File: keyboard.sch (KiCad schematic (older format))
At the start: 14 parts

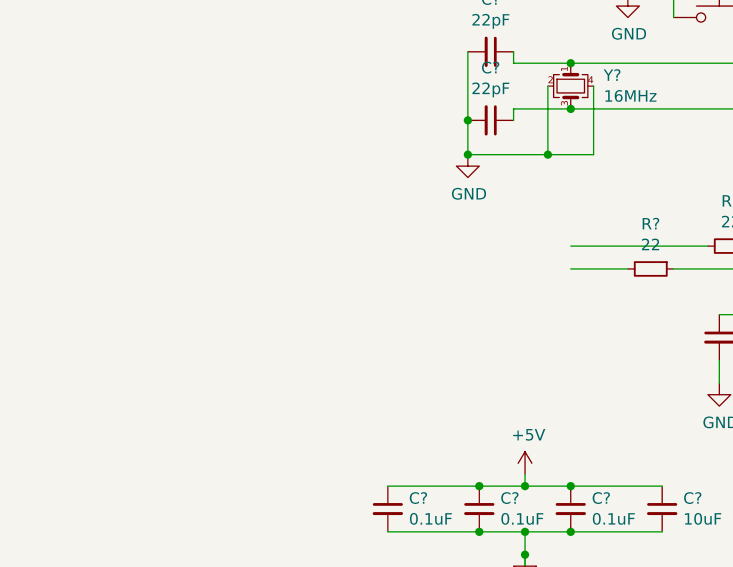
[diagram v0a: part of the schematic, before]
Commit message: Added usb controller
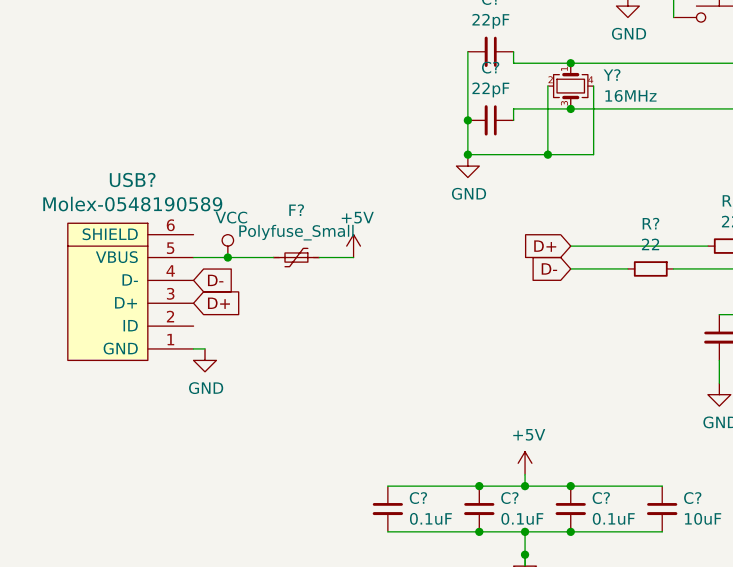
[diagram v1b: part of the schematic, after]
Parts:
- added F?: Polyfuse_Small, symbol Device:Polyfuse_Small
- added USB?: Molex-0548190589, symbol random-keyboard-parts:Molex-0548190589
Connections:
- net labels added: D+, D-, VCC
- wire segments 44 -> 48
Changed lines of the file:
@@
 Wire Wire Line
 	3550 3300 2950 3300
+$Comp
+L random-keyboard-parts:Molex-0548190589 USB?
+U 1 1 61618AFA
+P 1000 3550
+F 0 "USB?" V 1537 3517 60  0000 C CNN
+F 1 "Molex-0548190589" V 1431 3517 60  0000 C CNN
+F 2 "" H 1000 3550 60  0001 C CNN
+F 3 "" H 1000 3550 60  0001 C CNN
+	1    1000 3550
+	0    -1   -1   0
+$EndComp
+Text GLabel 2950 3300 0    50   Input ~ 0
+D+
+Text GLabel 2950 3400 0    50   Input ~ 0
+D-
+Text GLabel 1300 3450 2    50   Input ~ 0
+D-
+Text GLabel 1300 3550 2    50   Input ~ 0
+D+
+$Comp
+L power:GND #PWR?
+U 1 1 6161D0AE
+P 1350 3750
+F 0 "#PWR?" H 1350 3500 50  0001 C CNN
+F 1 "GND" H 1355 3577 50  0000 C CNN
+F 2 "" H 1350 3750 50  0001 C CNN
+F 3 "" H 1350 3750 50  0001 C CNN
+	1    1350 3750
+	1    0    0    -1
+$EndComp
+Wire Wire Line
+	1300 3750 1350 3750
+$Comp
+L Device:Polyfuse_Small F?
+U 1 1 6161E704
+P 1750 3350
+F 0 "F?" V 1545 3350 50  0000 C CNN
+F 1 "Polyfuse_Small" V 1636 3350 50  0000 C CNN
+F 2 "" H 1800 3150 50  0001 L CNN
+F 3 "~" H 1750 3350 50  0001 C CNN
+	1    1750 3350
+	0    1    1    0
+$EndComp
+$Comp
+L power:+5V #PWR?
+U 1 1 6161F616
+P 2000 3350
+F 0 "#PWR?" H 2000 3200 50  0001 C CNN
+F 1 "+5V" H 2015 3523 50  0000 C CNN
+F 2 "" H 2000 3350 50  0001 C CNN
+F 3 "" H 2000 3350 50  0001 C CNN
+	1    2000 3350
+	1    0    0    -1
+$EndComp
+$Comp
+L power:VCC #PWR?
+U 1 1 6162023C
+P 1450 3350
+F 0 "#PWR?" H 1450 3200 50  0001 C CNN
+F 1 "VCC" H 1467 3523 50  0000 C CNN
+F 2 "" H 1450 3350 50  0001 C CNN
+F 3 "" H 1450 3350 50  0001 C CNN
+	1    1450 3350
+	1    0    0    -1
+$EndComp
+Wire Wire Line
+	1300 3350 1450 3350
+Wire Wire Line
+	1850 3350 2000 3350
+Connection ~ 1450 3350
+Wire Wire Line
+	1450 3350 1650 3350
 $EndSCHEMATC

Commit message: Added all keys
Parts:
- added D? (x82): D_Small, symbol Device:D_Small
- added MX? (x82): MX-NoLED, symbol MX_Alps_Hybrid:MX-NoLED
- C1, C2, C3, C4, C5, C6, C7: renamed from C?; footprint (none) -> Capacitor_SMD:C_0805_2012Metric
- F1: renamed from F?; value Polyfuse_Small -> 500mA; footprint (none) -> Fuse:Fuse_1206_3216Metric
- R1, R2, R3, R4: renamed from R?; footprint (none) -> Resistor_SMD:R_0805_2012Metric
- Y1: renamed from Y?; footprint (none) -> Crystal:Crystal_SMD_3225-4Pin_3.2x2.5mm
- gave numbers to parts that had none: 3
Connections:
- new net: D?.2 (A), MX?.2 (ROW) (x82)

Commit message: Key wiring
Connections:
- net COL0: now reaches MX?.1 (COL)
- net COL0: now also MX?.1 (COL), MX?.1 (COL), MX?.1 (COL), MX?.1 (COL), MX?.1 (COL)
- net ROW0: now reaches D?.1 (K)
- net ROW0: now also D?.1 (K), D?.1 (K), D?.1 (K), D?.1 (K), D?.1 (K), D?.1 (K), D?.1 (K), D?.1 (K), D?.1 (K), D?.1 (K), D?.1 (K), D?.1 (K), D?.1 (K), D?.1 (K), D?.1 (K), D?.1 (K), D?.1 (K), D?.1 (K), D?.1 (K), D?.1 (K), D?.1 (K), D?.1 (K), D?.1 (K), D?.1 (K), D?.1 (K), D?.1 (K), D?.1 (K), D?.1 (K), D?.1 (K), D?.1 (K), D?.1 (K), D?.1 (K), D?.1 (K), D?.1 (K), D?.1 (K), D?.1 (K), D?.1 (K), D?.1 (K), D?.1 (K), D?.1 (K), D?.1 (K), D?.1 (K), D?.1 (K), D?.1 (K), D?.1 (K), D?.1 (K), D?.1 (K), D?.1 (K), D?.1 (K), D?.1 (K), D?.1 (K), D?.1 (K), D?.1 (K), D?.1 (K), D?.1 (K), D?.1 (K), D?.1 (K), D?.1 (K), D?.1 (K), D?.1 (K), D?.1 (K), D?.1 (K), D?.1 (K), D?.1 (K), D?.1 (K), D?.1 (K), D?.1 (K), D?.1 (K), D?.1 (K), D?.1 (K), D?.1 (K), D?.1 (K), D?.1 (K), D?.1 (K), D?.1 (K), D?.1 (K), D?.1 (K), D?.1 (K), D?.1 (K), D?.1 (K), D?.1 (K)
- net COL1: now reaches MX?.1 (COL)
- net COL1: now also MX?.1 (COL), MX?.1 (COL), MX?.1 (COL), MX?.1 (COL), MX?.1 (COL)
- net COL2: now reaches MX?.1 (COL)
- net COL2: now also MX?.1 (COL), MX?.1 (COL), MX?.1 (COL), MX?.1 (COL), MX?.1 (COL)
- net COL3: now reaches MX?.1 (COL)
- net COL3: now also MX?.1 (COL), MX?.1 (COL), MX?.1 (COL), MX?.1 (COL), MX?.1 (COL)
- net COL4: now reaches MX?.1 (COL)
- net COL4: now also MX?.1 (COL), MX?.1 (COL), MX?.1 (COL), MX?.1 (COL)
- net COL5: now reaches MX?.1 (COL)
- net COL5: now also MX?.1 (COL), MX?.1 (COL), MX?.1 (COL), MX?.1 (COL)
- net COL6: now reaches MX?.1 (COL)
- net COL6: now also MX?.1 (COL), MX?.1 (COL), MX?.1 (COL), MX?.1 (COL), MX?.1 (COL)
- net COL7: now reaches MX?.1 (COL)
- net COL7: now also MX?.1 (COL), MX?.1 (COL), MX?.1 (COL), MX?.1 (COL)
- net COL8: now reaches MX?.1 (COL)
- net COL8: now also MX?.1 (COL), MX?.1 (COL), MX?.1 (COL), MX?.1 (COL)
- net COL9: now reaches MX?.1 (COL)
- net COL9: now also MX?.1 (COL), MX?.1 (COL), MX?.1 (COL), MX?.1 (COL)
- net COL10: now reaches MX?.1 (COL)
- net COL10: now also MX?.1 (COL), MX?.1 (COL), MX?.1 (COL), MX?.1 (COL), MX?.1 (COL)
- net COL11: now reaches MX?.1 (COL)
- net COL11: now also MX?.1 (COL), MX?.1 (COL), MX?.1 (COL), MX?.1 (COL), MX?.1 (COL)
- net COL12: now reaches MX?.1 (COL)
- net COL12: now also MX?.1 (COL), MX?.1 (COL), MX?.1 (COL), MX?.1 (COL)
- net COL14: now reaches MX?.1 (COL)
- net COL14: now also MX?.1 (COL), MX?.1 (COL), MX?.1 (COL), MX?.1 (COL)
- net COL13: now reaches MX?.1 (COL)
- net COL13: now also MX?.1 (COL), MX?.1 (COL), MX?.1 (COL)
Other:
- moved on the sheet: C1, C2, C3, C4, C5, C6, C7, D?, F1, MX?, R1, R2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

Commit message: Key labeling
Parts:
- gave numbers to parts that had none: 82
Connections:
- net COL14: no longer MX_C4.1 (COL), MX_RIGHT.1 (COL)
- net ROW0: no longer D?.1 (K), D?.1 (K), D?.1 (K), D?.1 (K), D?.1 (K), D?.1 (K), D?.1 (K), D?.1 (K), D?.1 (K), D?.1 (K), D?.1 (K), D?.1 (K), D?.1 (K), D?.1 (K), D?.1 (K), D?.1 (K), D?.1 (K), D?.1 (K), D?.1 (K), D?.1 (K), D?.1 (K), D?.1 (K), D?.1 (K), D?.1 (K), D?.1 (K), D?.1 (K), D?.1 (K), D?.1 (K), D?.1 (K), D?.1 (K), D?.1 (K), D?.1 (K), D?.1 (K), D?.1 (K), D?.1 (K), D?.1 (K), D?.1 (K), D?.1 (K), D?.1 (K), D?.1 (K), D?.1 (K), D?.1 (K), D?.1 (K), D?.1 (K), D?.1 (K), D?.1 (K), D?.1 (K), D?.1 (K), D?.1 (K), D?.1 (K), D?.1 (K), D?.1 (K), D?.1 (K), D?.1 (K), D?.1 (K), D?.1 (K), D?.1 (K), D?.1 (K), D?.1 (K), D?.1 (K), D?.1 (K), D?.1 (K), D?.1 (K), D?.1 (K), D?.1 (K), D?.1 (K), D?.1 (K), D?.1 (K)
- new net: MX_C4.1 (COL), MX_RIGHT.1 (COL)
- new net ROW1: D?.1 (K), D?.1 (K), D?.1 (K), D?.1 (K), D?.1 (K), D?.1 (K), D?.1 (K), D?.1 (K), D?.1 (K), D?.1 (K), D?.1 (K), D?.1 (K), D?.1 (K), D?.1 (K), D?.1 (K)
- new net ROW2: D?.1 (K), D?.1 (K), D?.1 (K), D?.1 (K), D?.1 (K), D?.1 (K), D?.1 (K), D?.1 (K), D?.1 (K), D?.1 (K), D?.1 (K), D?.1 (K), D?.1 (K), D?.1 (K), D?.1 (K)
- new net ROW3: D?.1 (K), D?.1 (K), D?.1 (K), D?.1 (K), D?.1 (K), D?.1 (K), D?.1 (K), D?.1 (K), D?.1 (K), D?.1 (K), D?.1 (K), D?.1 (K), D?.1 (K), D?.1 (K)
- new net ROW4: D?.1 (K), D?.1 (K), D?.1 (K), D?.1 (K), D?.1 (K), D?.1 (K), D?.1 (K), D?.1 (K), D?.1 (K), D?.1 (K), D?.1 (K), D?.1 (K), D?.1 (K), D?.1 (K)
- new net ROW5: D?.1 (K), D?.1 (K), D?.1 (K), D?.1 (K), D?.1 (K), D?.1 (K), D?.1 (K), D?.1 (K), D?.1 (K), D?.1 (K)
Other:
- moved on the sheet: D?, MX_C3

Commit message: Key labeling
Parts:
- renumbered MX_' to MX_AP, MX_\ to MX_BSLASH, MX_, to MX_COMMA, MX_- to MX_DASH, MX_. to MX_DOT, MX_à to MX_aAcc, MX_è to MX_eAcc, MX_ì to MX_iAcc, MX_ò to MX_oAcc, MX_ù to MX_uAcc
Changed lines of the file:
@@
 	14250 5950 14200 5950
 $Comp
-L MX_Alps_Hybrid:MX-NoLED MX_\
+L MX_Alps_Hybrid:MX-NoLED MX_BSLASH
 U 1 1 61658D6B
 P 7250 4100
-F 0 "MX_\\" H 7283 4323 60  0000 C CNN
+F 0 "MX_BSLASH" H 7283 4323 60  0000 C CNN
 F 1 "MX-NoLED" H 7283 4249 20  0000 C CNN
 F 2 "" H 6625 4075 60  0001 C CNN
@@
 	11700 4300 11650 4300
 $Comp
-L MX_Alps_Hybrid:MX-NoLED MX_'
+L MX_Alps_Hybrid:MX-NoLED MX_AP
 U 1 1 61669E31
 P 12200 4100
-F 0 "MX_'" H 12233 4323 60  0000 C CNN
+F 0 "MX_AP" H 12233 4323 60  0000 C CNN
 F 1 "MX-NoLED" H 12233 4249 20  0000 C CNN
 F 2 "" H 11575 4075 60  0001 C CNN
@@
 	12150 4300 12100 4300
 $Comp
-L MX_Alps_Hybrid:MX-NoLED MX_ì
+L MX_Alps_Hybrid:MX-NoLED MX_iAcc
 U 1 1 61669E47
 P 12650 4100
-F 0 "MX_ì" H 12683 4323 60  0000 C CNN
+F 0 "MX_iAcc" H 12683 4323 60  0000 C CNN
 F 1 "MX-NoLED" H 12683 4249 20  0000 C CNN
 F 2 "" H 12025 4075 60  0001 C CNN
@@
 	12000 5150 11950 5150
 $Comp
-L MX_Alps_Hybrid:MX-NoLED MX_è
+L MX_Alps_Hybrid:MX-NoLED MX_eAcc
 U 1 1 61679772
 P 12500 4950
-F 0 "MX_è" H 12533 5173 60  0000 C CNN
+F 0 "MX_eAcc" H 12533 5173 60  0000 C CNN
 F 1 "MX-NoLED" H 12533 5099 20  0000 C CNN
 F 2 "" H 11875 4925 60  0001 C CNN
@@
 	11800 5950 11750 5950
 $Comp
-L MX_Alps_Hybrid:MX-NoLED MX_ò
+L MX_Alps_Hybrid:MX-NoLED MX_oAcc
 U 1 1 6169B213
 P 12300 5750
-F 0 "MX_ò" H 12333 5973 60  0000 C CNN
+F 0 "MX_oAcc" H 12333 5973 60  0000 C CNN
 F 1 "MX-NoLED" H 12333 5899 20  0000 C CNN
 F 2 "" H 11675 5725 60  0001 C CNN
@@
 	12250 5950 12200 5950
 $Comp
-L MX_Alps_Hybrid:MX-NoLED MX_à
+L MX_Alps_Hybrid:MX-NoLED MX_aAcc
 U 1 1 6169B229
 P 12750 5750
-F 0 "MX_à" H 12783 5973 60  0000 C CNN
+F 0 "MX_aAcc" H 12783 5973 60  0000 C CNN
 F 1 "MX-NoLED" H 12783 5899 20  0000 C CNN
 F 2 "" H 12125 5725 60  0001 C CNN
@@
 	12700 5950 12650 5950
 $Comp
-L MX_Alps_Hybrid:MX-NoLED MX_ù
+L MX_Alps_Hybrid:MX-NoLED MX_uAcc
 U 1 1 6169B23F
 P 13200 5750
-F 0 "MX_ù" H 13233 5973 60  0000 C CNN
+F 0 "MX_uAcc" H 13233 5973 60  0000 C CNN
 F 1 "MX-NoLED" H 13233 5899 20  0000 C CNN
 F 2 "" H 12575 5725 60  0001 C CNN
@@
 	11000 6700 10950 6700
 $Comp
-L MX_Alps_Hybrid:MX-NoLED MX_,
+L MX_Alps_Hybrid:MX-NoLED MX_COMMA
 U 1 1 6171E81A
 P 11500 6500
-F 0 "MX_," H 11533 6723 60  0000 C CNN
+F 0 "MX_COMMA" H 11533 6723 60  0000 C CNN
 F 1 "MX-NoLED" H 11533 6649 20  0000 C CNN
 F 2 "" H 10875 6475 60  0001 C CNN
@@
 	11450 6700 11400 6700
 $Comp
-L MX_Alps_Hybrid:MX-NoLED MX_.
+L MX_Alps_Hybrid:MX-NoLED MX_DOT
 U 1 1 6171E830
 P 11950 6500
-F 0 "MX_." H 11983 6723 60  0000 C CNN
+F 0 "MX_DOT" H 11983 6723 60  0000 C CNN
 F 1 "MX-NoLED" H 11983 6649 20  0000 C CNN
 F 2 "" H 11325 6475 60  0001 C CNN
@@
 	11900 6700 11850 6700
 $Comp
-L MX_Alps_Hybrid:MX-NoLED MX_-
+L MX_Alps_Hybrid:MX-NoLED MX_DASH
 U 1 1 6171E846
 P 12400 6500
-F 0 "MX_-" H 12433 6723 60  0000 C CNN
+F 0 "MX_DASH" H 12433 6723 60  0000 C CNN
 F 1 "MX-NoLED" H 12433 6649 20  0000 C CNN
 F 2 "" H 11775 6475 60  0001 C CNN

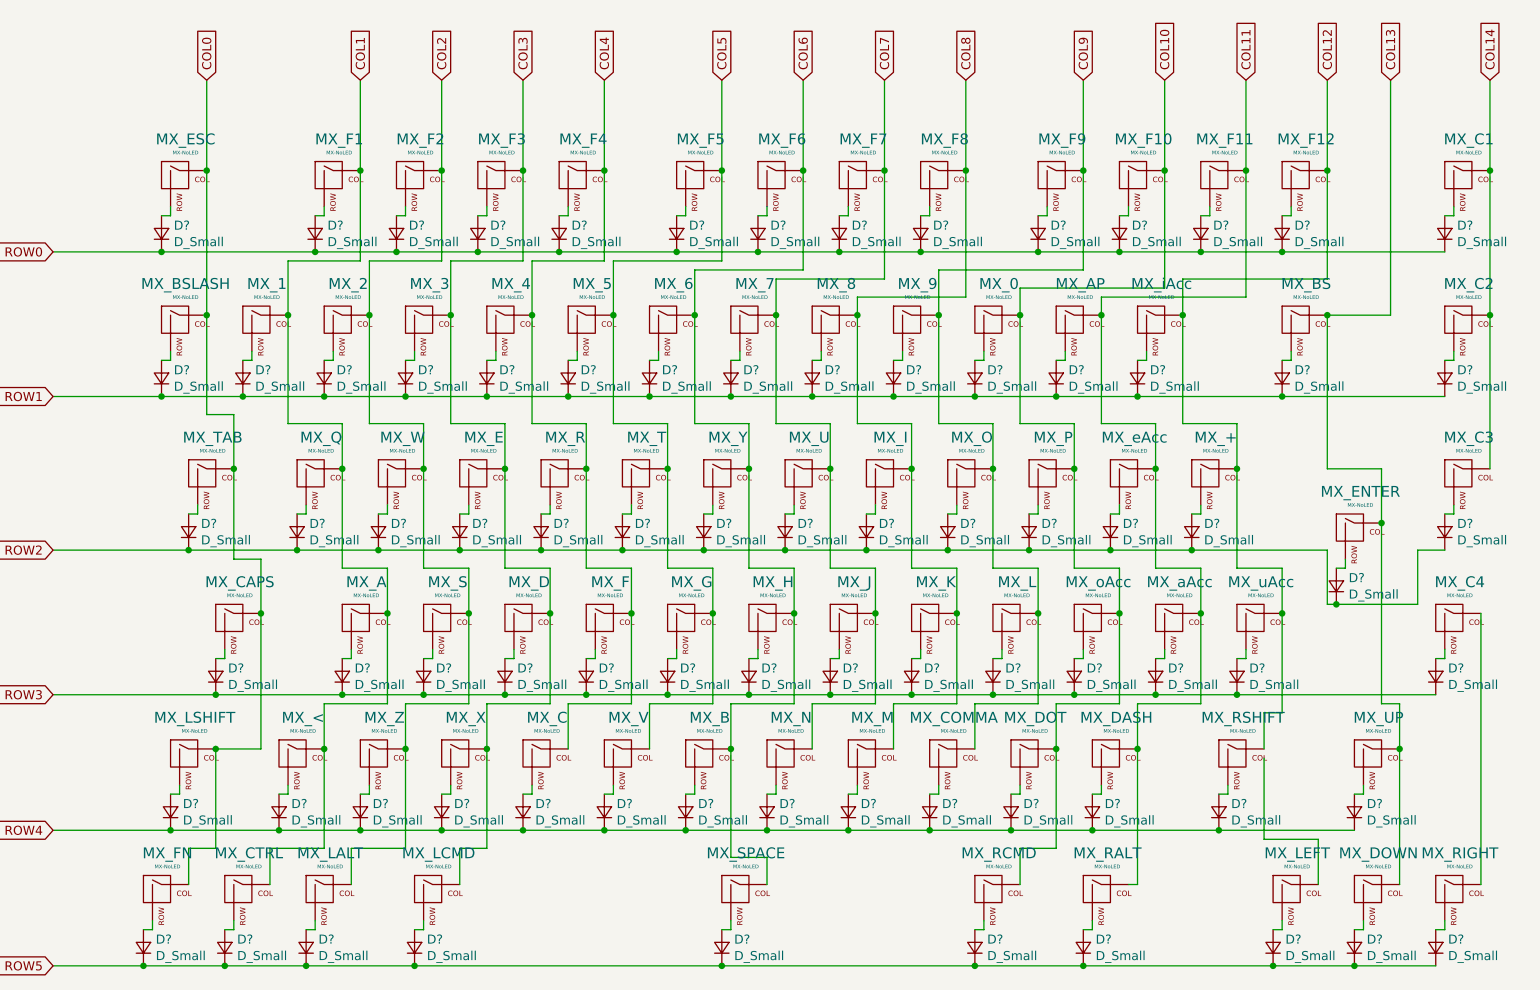
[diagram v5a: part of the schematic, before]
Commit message: Test importing schematics in pcb
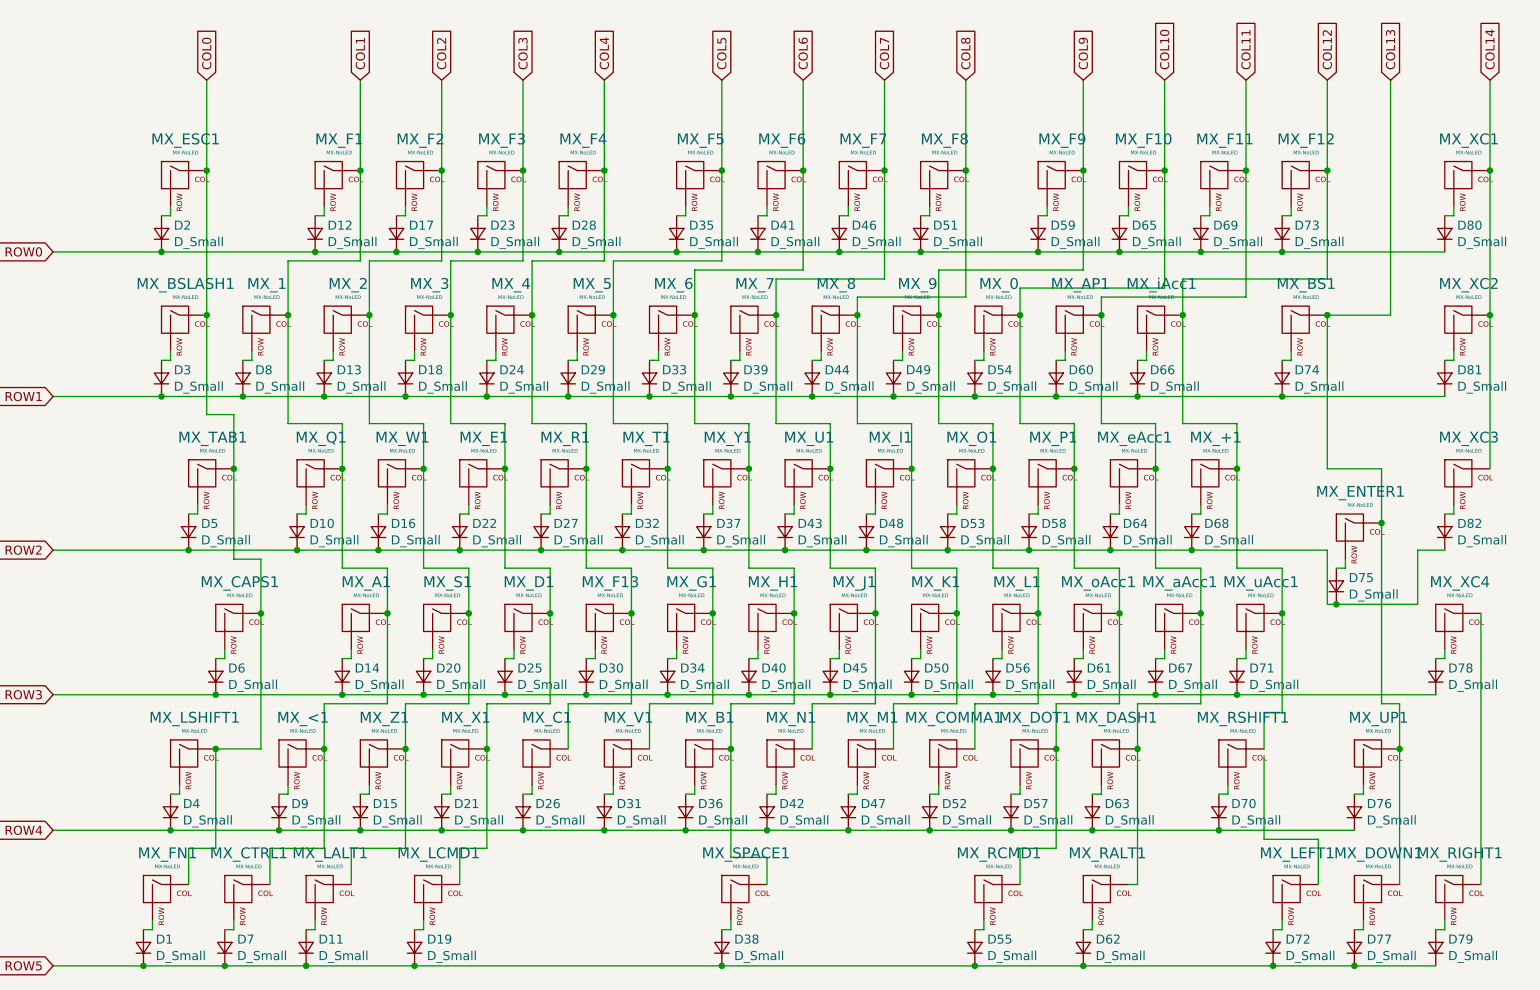
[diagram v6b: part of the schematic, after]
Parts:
- D1, D10, D11, D12, D13, D14, D15, D16, D17, D18, D19, D2, D20, D21, D22, D23, D24, D25, D26, D27, D28, D29, D3, D30, D31, D32, D33, D34, D35, D36, D37, D38, D39, D4, D40, D41, D42, D43, D44, D45, D46, D47, D48, D49, D5, D50, D51, D52, D53, D54, D55, D56, D57, D58, D59, D6, D60, D61, D62, D63, D64, D65, D66, D67, D68, D69, D7, D70, D71, D72, D73, D74, D75, D76, D77, D78, D79, D8, D80, D81, D82, D9: renamed from D?; footprint (none) -> Diode_SMD:D_SOD-123
- MX_+1: renamed from MX_+; footprint (none) -> MX_Alps_Hybrid:MX-1U-NoLED
- MX_0, MX_1, MX_2, MX_3, MX_4, MX_5, MX_6, MX_7, MX_8, MX_9, MX_F1, MX_F10, MX_F11, MX_F12, MX_F2, MX_F3, MX_F4, MX_F5, MX_F6, MX_F7, MX_F8, MX_F9: footprint (none) -> MX_Alps_Hybrid:MX-1U-NoLED
- MX_<1: renamed from MX_<; footprint (none) -> MX_Alps_Hybrid:MX-1U-NoLED
- MX_A1: renamed from MX_A; footprint (none) -> MX_Alps_Hybrid:MX-1U-NoLED
- MX_AP1: renamed from MX_AP; footprint (none) -> MX_Alps_Hybrid:MX-1U-NoLED
- MX_B1: renamed from MX_B; footprint (none) -> MX_Alps_Hybrid:MX-1U-NoLED
- MX_BS1: renamed from MX_BS; footprint (none) -> MX_Alps_Hybrid:MX-2U-NoLED
- MX_BSLASH1: renamed from MX_BSLASH; footprint (none) -> MX_Alps_Hybrid:MX-1U-NoLED
- MX_C1: renamed from MX_C; footprint (none) -> MX_Alps_Hybrid:MX-1U-NoLED
- MX_CAPS1: renamed from MX_CAPS; footprint (none) -> MX_Alps_Hybrid:MX-1.75U-NoLED
- MX_COMMA1: renamed from MX_COMMA; footprint (none) -> MX_Alps_Hybrid:MX-1U-NoLED
- MX_CTRL1: renamed from MX_CTRL; footprint (none) -> MX_Alps_Hybrid:MX-1U-NoLED
- MX_D1: renamed from MX_D; footprint (none) -> MX_Alps_Hybrid:MX-1U-NoLED
- MX_DASH1: renamed from MX_DASH; footprint (none) -> MX_Alps_Hybrid:MX-1U-NoLED
- MX_DOT1: renamed from MX_DOT; footprint (none) -> MX_Alps_Hybrid:MX-1U-NoLED
- MX_DOWN1: renamed from MX_DOWN; footprint (none) -> MX_Alps_Hybrid:MX-1U-NoLED
- MX_E1: renamed from MX_E; footprint (none) -> MX_Alps_Hybrid:MX-1U-NoLED
- MX_ENTER1: renamed from MX_ENTER; footprint (none) -> MX_Alps_Hybrid:MX-ISO
- MX_ESC1: renamed from MX_ESC; footprint (none) -> MX_Alps_Hybrid:MX-1U-NoLED
- MX_F13: renamed from MX_F; footprint (none) -> MX_Alps_Hybrid:MX-1U-NoLED
- MX_FN1: renamed from MX_FN; footprint (none) -> MX_Alps_Hybrid:MX-1U-NoLED
- MX_G1: renamed from MX_G; footprint (none) -> MX_Alps_Hybrid:MX-1U-NoLED
- MX_H1: renamed from MX_H; footprint (none) -> MX_Alps_Hybrid:MX-1U-NoLED
- MX_I1: renamed from MX_I; footprint (none) -> MX_Alps_Hybrid:MX-1U-NoLED
- MX_J1: renamed from MX_J; footprint (none) -> MX_Alps_Hybrid:MX-1U-NoLED
- MX_K1: renamed from MX_K; footprint (none) -> MX_Alps_Hybrid:MX-1U-NoLED
- MX_L1: renamed from MX_L; footprint (none) -> MX_Alps_Hybrid:MX-1U-NoLED
- MX_LALT1: renamed from MX_LALT; footprint (none) -> MX_Alps_Hybrid:MX-1U-NoLED
- MX_LCMD1: renamed from MX_LCMD; footprint (none) -> MX_Alps_Hybrid:MX-1.25U-NoLED
- MX_LEFT1: renamed from MX_LEFT; footprint (none) -> MX_Alps_Hybrid:MX-1U-NoLED
- MX_LSHIFT1: renamed from MX_LSHIFT; footprint (none) -> MX_Alps_Hybrid:MX-1.25U-NoLED
- MX_M1: renamed from MX_M; footprint (none) -> MX_Alps_Hybrid:MX-1U-NoLED
- MX_N1: renamed from MX_N; footprint (none) -> MX_Alps_Hybrid:MX-1U-NoLED
- MX_O1: renamed from MX_O; footprint (none) -> MX_Alps_Hybrid:MX-1U-NoLED
- MX_P1: renamed from MX_P; footprint (none) -> MX_Alps_Hybrid:MX-1U-NoLED
- MX_Q1: renamed from MX_Q; footprint (none) -> MX_Alps_Hybrid:MX-1U-NoLED
- MX_R1: renamed from MX_R; footprint (none) -> MX_Alps_Hybrid:MX-1U-NoLED
- MX_RALT1: renamed from MX_RALT; footprint (none) -> MX_Alps_Hybrid:MX-1.25U-NoLED
- MX_RCMD1: renamed from MX_RCMD; footprint (none) -> MX_Alps_Hybrid:MX-1.5U-NoLED
- MX_RIGHT1: renamed from MX_RIGHT; footprint (none) -> MX_Alps_Hybrid:MX-1U-NoLED
- MX_RSHIFT1: renamed from MX_RSHIFT; footprint (none) -> MX_Alps_Hybrid:MX-1.75U-NoLED
- MX_S1: renamed from MX_S; footprint (none) -> MX_Alps_Hybrid:MX-1U-NoLED
- MX_SPACE1: renamed from MX_SPACE; footprint (none) -> MX_Alps_Hybrid:MX-6U-NoLED
- MX_T1: renamed from MX_T; footprint (none) -> MX_Alps_Hybrid:MX-1U-NoLED
- MX_TAB1: renamed from MX_TAB; footprint (none) -> MX_Alps_Hybrid:MX-1.5U-NoLED
- MX_U1: renamed from MX_U; footprint (none) -> MX_Alps_Hybrid:MX-1U-NoLED
- MX_UP1: renamed from MX_UP; footprint (none) -> MX_Alps_Hybrid:MX-1U-NoLED
- MX_V1: renamed from MX_V; footprint (none) -> MX_Alps_Hybrid:MX-1U-NoLED
- MX_W1: renamed from MX_W; footprint (none) -> MX_Alps_Hybrid:MX-1U-NoLED
- MX_X1: renamed from MX_X; footprint (none) -> MX_Alps_Hybrid:MX-1U-NoLED
- MX_XC1: renamed from MX_C1; footprint (none) -> MX_Alps_Hybrid:MX-1U-NoLED
- MX_XC2: renamed from MX_C2; footprint (none) -> MX_Alps_Hybrid:MX-1U-NoLED
- MX_XC3: renamed from MX_C3; footprint (none) -> MX_Alps_Hybrid:MX-1U-NoLED
- MX_XC4: renamed from MX_C4; footprint (none) -> MX_Alps_Hybrid:MX-1U-NoLED
- MX_Y1: renamed from MX_Y; footprint (none) -> MX_Alps_Hybrid:MX-1U-NoLED
- MX_Z1: renamed from MX_Z; footprint (none) -> MX_Alps_Hybrid:MX-1U-NoLED
- MX_aAcc1: renamed from MX_aAcc; footprint (none) -> MX_Alps_Hybrid:MX-1U-NoLED
- MX_eAcc1: renamed from MX_eAcc; footprint (none) -> MX_Alps_Hybrid:MX-1U-NoLED
- MX_iAcc1: renamed from MX_iAcc; footprint (none) -> MX_Alps_Hybrid:MX-1U-NoLED
- MX_oAcc1: renamed from MX_oAcc; footprint (none) -> MX_Alps_Hybrid:MX-1U-NoLED
- MX_uAcc1: renamed from MX_uAcc; footprint (none) -> MX_Alps_Hybrid:MX-1U-NoLED
- SW1: footprint (none) -> random-keyboard-parts:SKQG-1155865
- USB1: footprint (none) -> random-keyboard-parts:Molex-0548190589
